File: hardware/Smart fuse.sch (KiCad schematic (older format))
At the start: 2 parts, among them U12 SMART FUSE

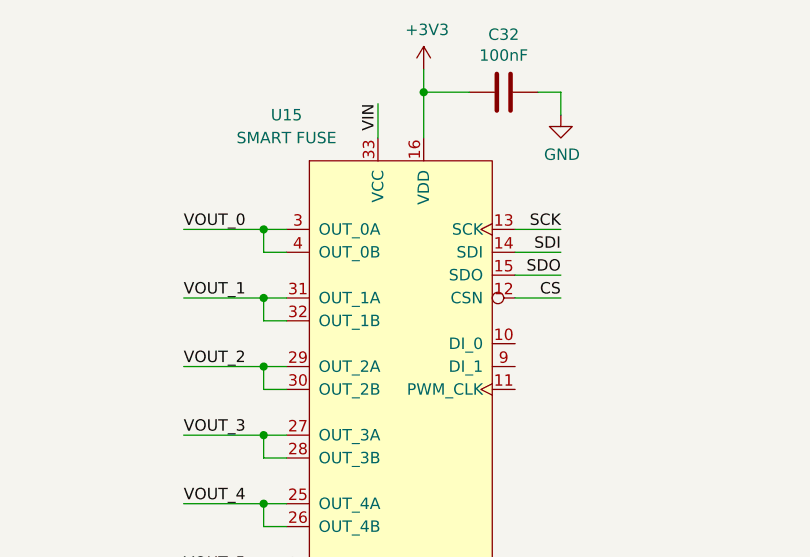
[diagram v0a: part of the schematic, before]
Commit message: Updated to be compatible with KiCad 6.0.0, changed chematics layouts to fit in A4 worksheet and finished routing the rest of the signals.
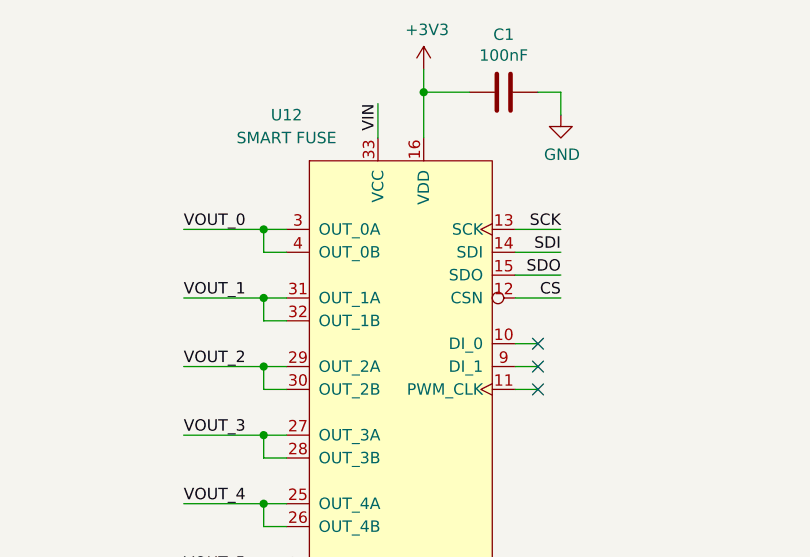
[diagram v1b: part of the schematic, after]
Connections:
- no-connect marks 0 -> 3
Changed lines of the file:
@@
 $Descr A4 11693 8268
 encoding utf-8
-Sheet 12 20
+Sheet 3 24
 Title ""
 Date ""
@@
 AR Path="/61A74311/6197C194" Ref="C31"  Part="1"
 AR Path="/61DC1767/6197C194" Ref="C32"  Part="1"
-F 0 "C32" V 5898 2700 50  0000 C CNN
+F 0 "C1" V 5898 2700 50  0000 C CNN
 F 1 "100nF" V 5989 2700 50  0000 C CNN
 F 2 "Capacitor_SMD:C_0603_1608Metric" H 6188 2550 50  0001 C CNN
@@
 AR Path="/61A74311/61B9BFD9" Ref="U14"  Part="1"
 AR Path="/61DC1767/61B9BFD9" Ref="U15"  Part="1"
-F 0 "U15" H 5200 3200 50  0000 C CNN
+F 0 "U12" H 5200 3200 50  0000 C CNN
 F 1 "SMART FUSE" H 5200 3100 50  0000 C CNN
 F 2 "VN9D30Q100F:QFN-32_EP_6x6_Pitch0.5mm" H 6100 3150 50  0001 C CNN
@@
 	1    0    0    -1
 $EndComp
+Wire Wire Line
+	6300 3800 6200 3800
+NoConn ~ 6300 3800
+Wire Wire Line
+	6300 3900 6200 3900
+NoConn ~ 6300 3900
+Wire Wire Line
+	6300 4000 6200 4000
+NoConn ~ 6300 4000
 $EndSCHEMATC
